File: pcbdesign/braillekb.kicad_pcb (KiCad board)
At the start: 2 copper layers, 180.3 x 38.1 mm, 17 parts, among them SW11 SW_Push, SW12 SW_Push, SW23 SW_Push, SW24 SW_Push, SW47 SW_Push, SW48 SW_Push, SW55 SW_Push, SW56 SW_Push, U11 ProMicro

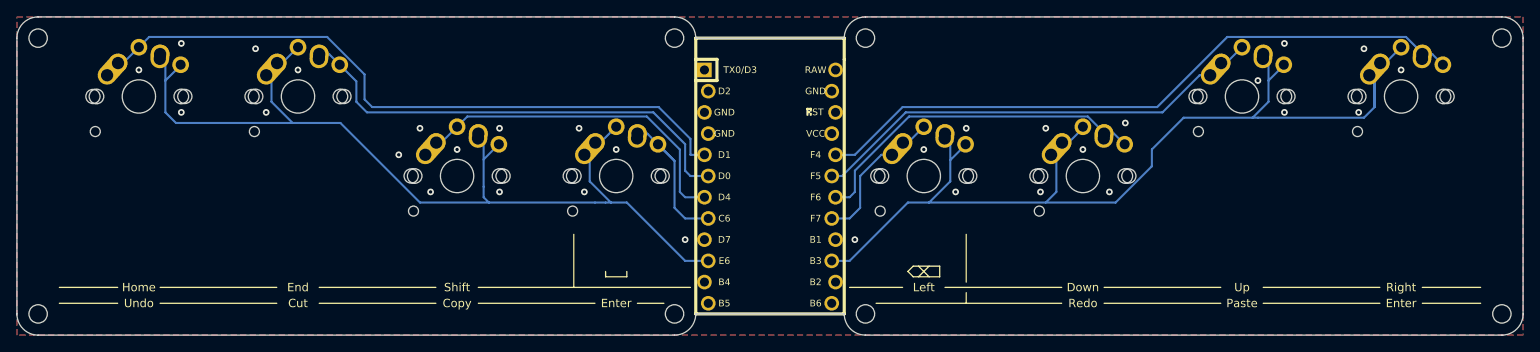
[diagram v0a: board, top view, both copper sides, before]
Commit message: minimize a width
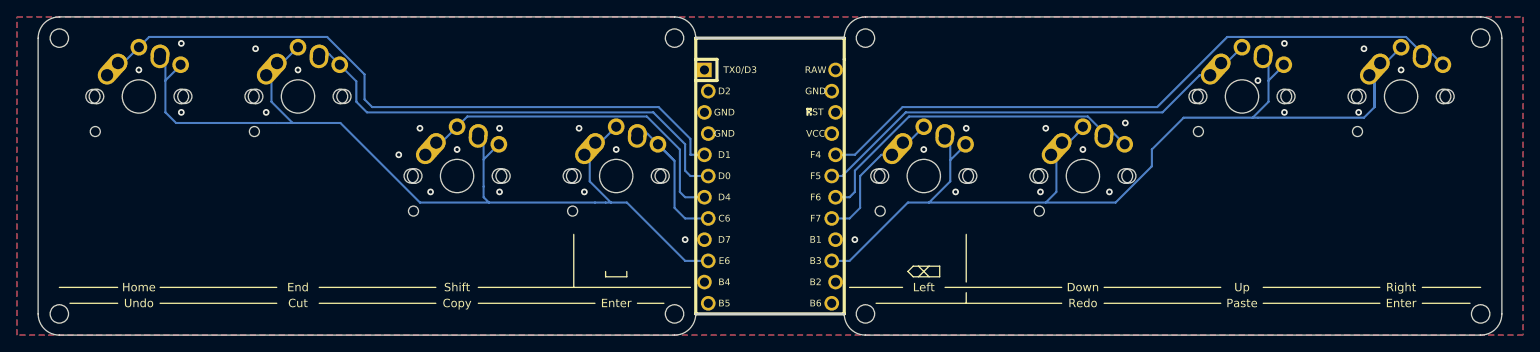
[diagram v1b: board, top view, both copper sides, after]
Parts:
- moved H1 2.54 mm to (27.3, 123.2)
- moved H5 2.54 mm to (27.3, 156.2)
- moved H4 2.54 mm to (197.5, 123.2)
- moved H7 2.54 mm to (197.5, 156.2)
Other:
- board size 180.3 x 38.1 mm -> 175.3 x 38.1 mm
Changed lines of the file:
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@@
   (page A4)
   (layers
-    (0 F.Cu signal)
-    (31 B.Cu signal)
+    (0 F.Cu signal hide)
+    (31 B.Cu signal hide)
     (32 B.Adhes user)
     (33 F.Adhes user)
@@
     (pad_to_mask_clearance 0.051)
     (solder_mask_min_width 0.25)
-    (aux_axis_origin 22.225 158.75)
+    (aux_axis_origin 24.765 158.75)
     (visible_elements 7FFFFFFF)
     (pcbplotparams
@@
   )
   (module MountingHole:MountingHole_2.2mm_M2 (layer F.Cu)
-    (at 200.025 156.21)
+    (at 197.485 156.21)
     (descr "Mounting Hole 2.2mm, no annular, M2")
     (tags "mounting hole 2.2mm no annular m2")
@@
   )
   (module MountingHole:MountingHole_2.2mm_M2 (layer F.Cu)
-    (at 24.765 156.21)
+    (at 27.305 156.21)
     (descr "Mounting Hole 2.2mm, no annular, M2")
     (tags "mounting hole 2.2mm no annular m2")
@@
   )
   (module MountingHole:MountingHole_2.2mm_M2 (layer F.Cu)
-    (at 200.025 123.19)
+    (at 197.485 123.19)
     (descr "Mounting Hole 2.2mm, no annular, M2")
     (tags "mounting hole 2.2mm no annular m2")
@@
   )
   (module MountingHole:MountingHole_2.2mm_M2 (layer F.Cu)
-    (at 24.765 123.19)
+    (at 27.305 123.19)
     (descr "Mounting Hole 2.2mm, no annular, M2")
     (tags "mounting hole 2.2mm no annular m2")
@@
   (gr_line (start 103.505 123.19) (end 121.285 123.19) (layer Edge.Cuts) (width 0.05))
   (gr_line (start 103.505 156.21) (end 121.285 156.21) (layer Edge.Cuts) (width 0.05))
-  (gr_line (start 100.965 158.75) (end 24.765 158.75) (layer Edge.Cuts) (width 0.05))
-  (gr_line (start 200.025 158.75) (end 123.825 158.75) (layer Edge.Cuts) (width 0.05))
-  (gr_line (start 200.025 120.65) (end 123.825 120.65) (layer Edge.Cuts) (width 0.05))
+  (gr_line (start 100.965 158.75) (end 27.305 158.75) (layer Edge.Cuts) (width 0.05))
+  (gr_line (start 197.485 158.75) (end 123.825 158.75) (layer Edge.Cuts) (width 0.05))
+  (gr_line (start 197.485 120.65) (end 123.825 120.65) (layer Edge.Cuts) (width 0.05))
   (gr_arc (start 100.965 123.19) (end 103.505 123.19) (angle -90) (layer Edge.Cuts) (width 0.05))
   (gr_arc (start 100.965 156.21) (end 100.965 158.75) (angle -90) (layer Edge.Cuts) (width 0.05))
@@
   (gr_line (start 166.37 154.94) (end 152.4 154.94) (layer F.SilkS) (width 0.12))
   (gr_line (start 185.42 154.94) (end 171.45 154.94) (layer F.SilkS) (width 0.12))
-  (gr_line (start 197.485 154.94) (end 190.5 154.94) (layer F.SilkS) (width 0.12))
+  (gr_line (start 196.215 154.94) (end 190.5 154.94) (layer F.SilkS) (width 0.12))
   (gr_line (start 190.5 153.035) (end 197.485 153.035) (layer F.SilkS) (width 0.12))
   (gr_line (start 171.45 153.035) (end 185.42 153.035) (layer F.SilkS) (width 0.12))
@@
   (gr_line (start 58.42 154.94) (end 72.39 154.94) (layer F.SilkS) (width 0.12))
   (gr_line (start 39.37 154.94) (end 53.34 154.94) (layer F.SilkS) (width 0.12))
-  (gr_line (start 27.305 154.94) (end 34.29 154.94) (layer F.SilkS) (width 0.12))
+  (gr_line (start 28.575 154.94) (end 34.29 154.94) (layer F.SilkS) (width 0.12))
   (gr_line (start 34.29 153.035) (end 27.305 153.035) (layer F.SilkS) (width 0.12))
   (gr_line (start 53.34 153.035) (end 39.37 153.035) (layer F.SilkS) (width 0.12))
@@
     (effects (font (size 1 1) (thickness 0.15)))
   )
-  (gr_arc (start 24.765 156.21) (end 22.225 156.21) (angle -90) (layer Edge.Cuts) (width 0.05))
-  (gr_arc (start 24.765 123.19) (end 24.765 120.65) (angle -90) (layer Edge.Cuts) (width 0.05))
-  (gr_arc (start 200.025 123.19) (end 202.565 123.19) (angle -90) (layer Edge.Cuts) (width 0.05))
-  (gr_arc (start 200.025 156.21) (end 200.025 158.75) (angle -90) (layer Edge.Cuts) (width 0.05))
+  (gr_arc (start 27.305 156.21) (end 24.765 156.21) (angle -90) (layer Edge.Cuts) (width 0.05))
+  (gr_arc (start 27.305 123.19) (end 27.305 120.65) (angle -90) (layer Edge.Cuts) (width 0.05))
+  (gr_arc (start 197.485 123.19) (end 200.025 123.19) (angle -90) (layer Edge.Cuts) (width 0.05))
+  (gr_arc (start 197.485 156.21) (end 197.485 158.75) (angle -90) (layer Edge.Cuts) (width 0.05))
   (dimension 38.1 (width 0.12) (layer F.Fab)
-    (gr_text "38.100 mm" (at 16.51 139.7 270) (layer F.Fab)
-      (effects (font (size 1 1) (thickness 0.15)))
-    )
-    (feature1 (pts (xy 22.225 158.75) (xy 17.193579 158.75)))
-    (feature2 (pts (xy 22.225 120.65) (xy 17.193579 120.65)))
-    (crossbar (pts (xy 17.78 120.65) (xy 17.78 158.75)))
-    (arrow1a (pts (xy 17.78 158.75) (xy 17.193579 157.623496)))
-    (arrow1b (pts (xy 17.78 158.75) (xy 18.366421 157.623496)))
-    (arrow2a (pts (xy 17.78 120.65) (xy 17.193579 121.776504)))
-    (arrow2b (pts (xy 17.78 120.65) (xy 18.366421 121.776504)))
-  )
-  (dimension 180.34 (width 0.12) (layer F.Fab)
-    (gr_text "180.340 mm" (at 112.395 114.935) (layer F.Fab)
-      (effects (font (size 1 1) (thickness 0.15)))
-    )
-    (feature1 (pts (xy 22.225 120.65) (xy 22.225 115.618579)))
-    (feature2 (pts (xy 202.565 120.65) (xy 202.565 115.618579)))
-    (crossbar (pts (xy 202.565 116.205) (xy 22.225 116.205)))
-    (arrow1a (pts (xy 22.225 116.205) (xy 23.351504 115.618579)))
-    (arrow1b (pts (xy 22.225 116.205) (xy 23.351504 116.791421)))
-    (arrow2a (pts (xy 202.565 116.205) (xy 201.438496 115.618579)))
-    (arrow2b (pts (xy 202.565 116.205) (xy 201.438496 116.791421)))
-  )
-  (gr_line (start 202.565 156.21) (end 202.565 123.19) (layer Edge.Cuts) (width 0.05))
-  (gr_line (start 22.225 123.19) (end 22.225 156.21) (layer Edge.Cuts) (width 0.05))
-  (gr_line (start 100.965 120.65) (end 24.765 120.65) (layer Edge.Cuts) (width 0.05))
+    (gr_text "38.100 mm" (at 19.05 139.7 270) (layer F.Fab)
+      (effects (font (size 1 1) (thickness 0.15)))
+    )
+    (feature1 (pts (xy 24.765 158.75) (xy 19.733579 158.75)))
+    (feature2 (pts (xy 24.765 120.65) (xy 19.733579 120.65)))
+    (crossbar (pts (xy 20.32 120.65) (xy 20.32 158.75)))
+    (arrow1a (pts (xy 20.32 158.75) (xy 19.733579 157.623496)))
+    (arrow1b (pts (xy 20.32 158.75) (xy 20.906421 157.623496)))
+    (arrow2a (pts (xy 20.32 120.65) (xy 19.733579 121.776504)))
+    (arrow2b (pts (xy 20.32 120.65) (xy 20.906421 121.776504)))
+  )
+  (dimension 175.26 (width 0.12) (layer F.Fab)
+    (gr_text "175.260 mm" (at 112.395 114.935) (layer F.Fab)
+      (effects (font (size 1 1) (thickness 0.15)))
+    )
+    (feature1 (pts (xy 24.765 120.65) (xy 24.765 115.618579)))
+    (feature2 (pts (xy 200.025 120.65) (xy 200.025 115.618579)))
+    (crossbar (pts (xy 200.025 116.205) (xy 24.765 116.205)))
+    (arrow1a (pts (xy 24.765 116.205) (xy 25.891504 115.618579)))
+    (arrow1b (pts (xy 24.765 116.205) (xy 25.891504 116.791421)))
+    (arrow2a (pts (xy 200.025 116.205) (xy 198.898496 115.618579)))
+    (arrow2b (pts (xy 200.025 116.205) (xy 198.898496 116.791421)))
+  )
+  (gr_line (start 200.025 156.21) (end 200.025 123.19) (layer Edge.Cuts) (width 0.05))
+  (gr_line (start 24.765 123.19) (end 24.765 156.21) (layer Edge.Cuts) (width 0.05))
+  (gr_line (start 100.965 120.65) (end 27.305 120.65) (layer Edge.Cuts) (width 0.05))
   (segment (start 105.0036 149.86) (end 102.235 149.86) (width 0.25) (layer B.Cu) (net 1))
   (segment (start 102.235 149.86) (end 95.25 142.875) (width 0.25) (layer B.Cu) (net 1))

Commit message: modify route
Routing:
- net C4: track 18.7 -> 16.0 mm
- net C6: track 41.4 -> 43.0 mm
- net C1: track 81.7 -> 81.0 mm

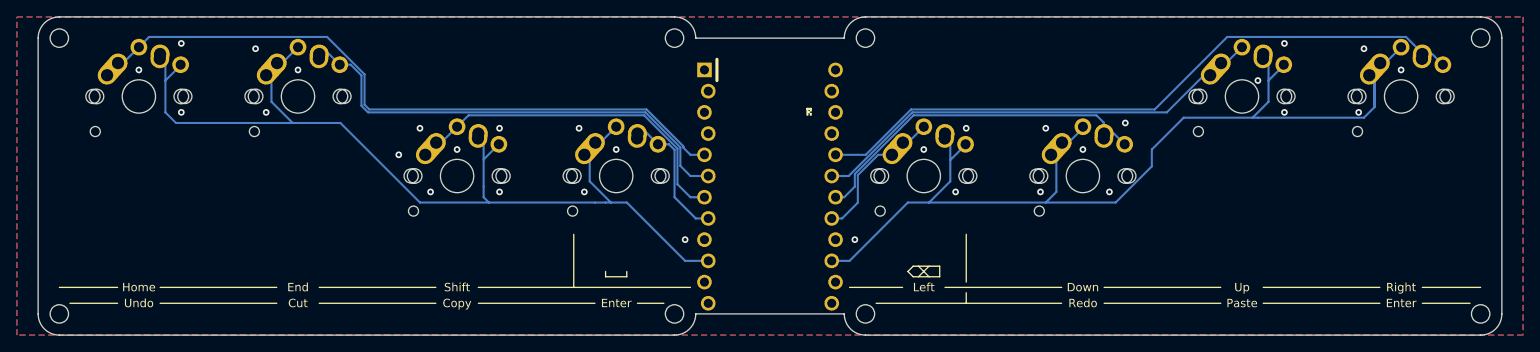
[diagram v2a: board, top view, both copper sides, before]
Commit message: widen 50mil on center
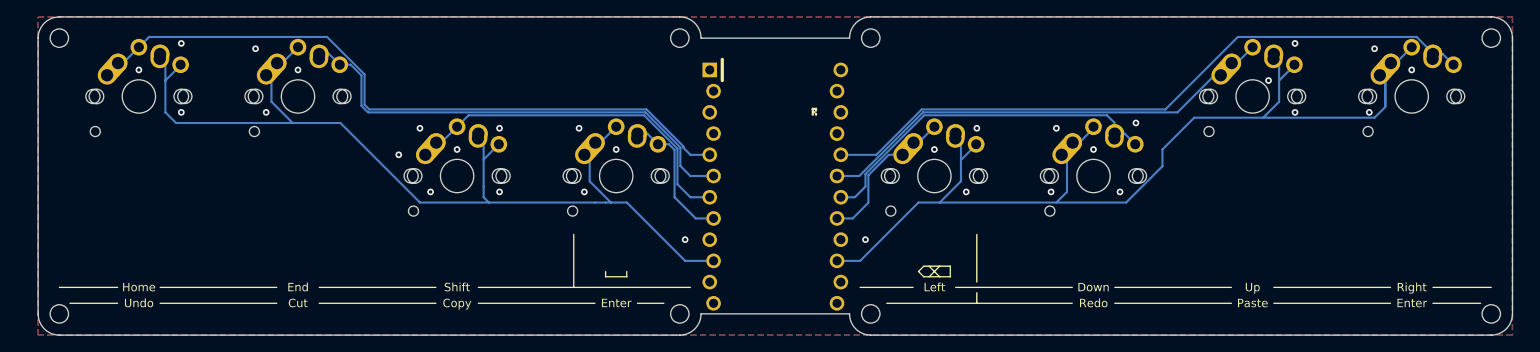
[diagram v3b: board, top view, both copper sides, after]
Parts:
- moved SW47 1.27 mm to (170.2, 130.2)
- moved SW55 1.27 mm to (132.1, 139.7)
- moved H4 1.27 mm to (198.8, 123.2)
- moved H7 1.27 mm to (198.8, 156.2)
- moved SW48 1.27 mm to (189.2, 130.2)
- moved SW56 1.27 mm to (151.1, 139.7)
- moved U11 0.64 mm to (113.0, 141.0)
- moved H2 0.63 mm to (101.6, 123.2)
- moved H3 0.63 mm to (124.5, 123.2)
- moved H6 0.63 mm to (101.6, 156.2)
- moved H8 0.63 mm to (124.5, 156.2)
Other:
- board size 175.3 x 38.1 mm -> 176.5 x 38.1 mm

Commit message: widen clearance to 0.25
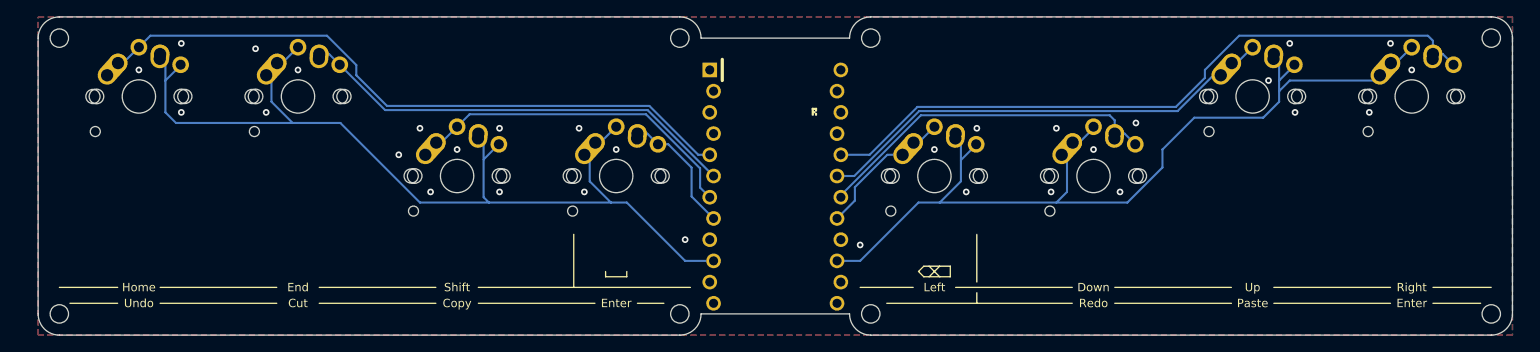
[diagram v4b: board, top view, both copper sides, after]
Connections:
- U11 pad 1: (no net) -> unconnected-(U11-Pad1)
- U11 pad 11: (no net) -> unconnected-(U11-Pad11)
- U11 pad 12: (no net) -> unconnected-(U11-Pad12)
- U11 pad 13: (no net) -> unconnected-(U11-Pad13)
- U11 pad 14: (no net) -> unconnected-(U11-Pad14)
- U11 pad 16: (no net) -> unconnected-(U11-Pad16)
- U11 pad 2: (no net) -> unconnected-(U11-Pad2)
- U11 pad 21: (no net) -> unconnected-(U11-Pad21)
- U11 pad 22: (no net) -> unconnected-(U11-Pad22)
- U11 pad 24: (no net) -> unconnected-(U11-Pad24)
- U11 pad 9: (no net) -> unconnected-(U11-Pad9)
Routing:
- net R4: track 120.6 -> 108.1 mm
- net C2: track 56.1 -> 53.3 mm
- net C8: track 79.8 -> 82.2 mm
- net C5: track 18.2 -> 16.7 mm
- net C6: track 43.0 -> 41.6 mm
- net C1: track 81.0 -> 80.3 mm
- net C7: track 55.5 -> 54.8 mm
- net C4: track 16.0 -> 15.3 mm
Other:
- net class Default removed
- rule pad_to_mask_clearance: 0.051 -> 0
- board text added: "JLCJLCJLC"
